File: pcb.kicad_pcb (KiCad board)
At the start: 4 copper layers, 26 x 25.6 mm, 39 parts, among them J1 TC2030-NL, J2 Conn_01x04, P1 USB_C_Plug, SW1 BOOT, U1 WE-TVS-82400102, U2 TCAN1042HGVDQ1, U3 STM32G431CBUx, U9 AP2112K-3.3

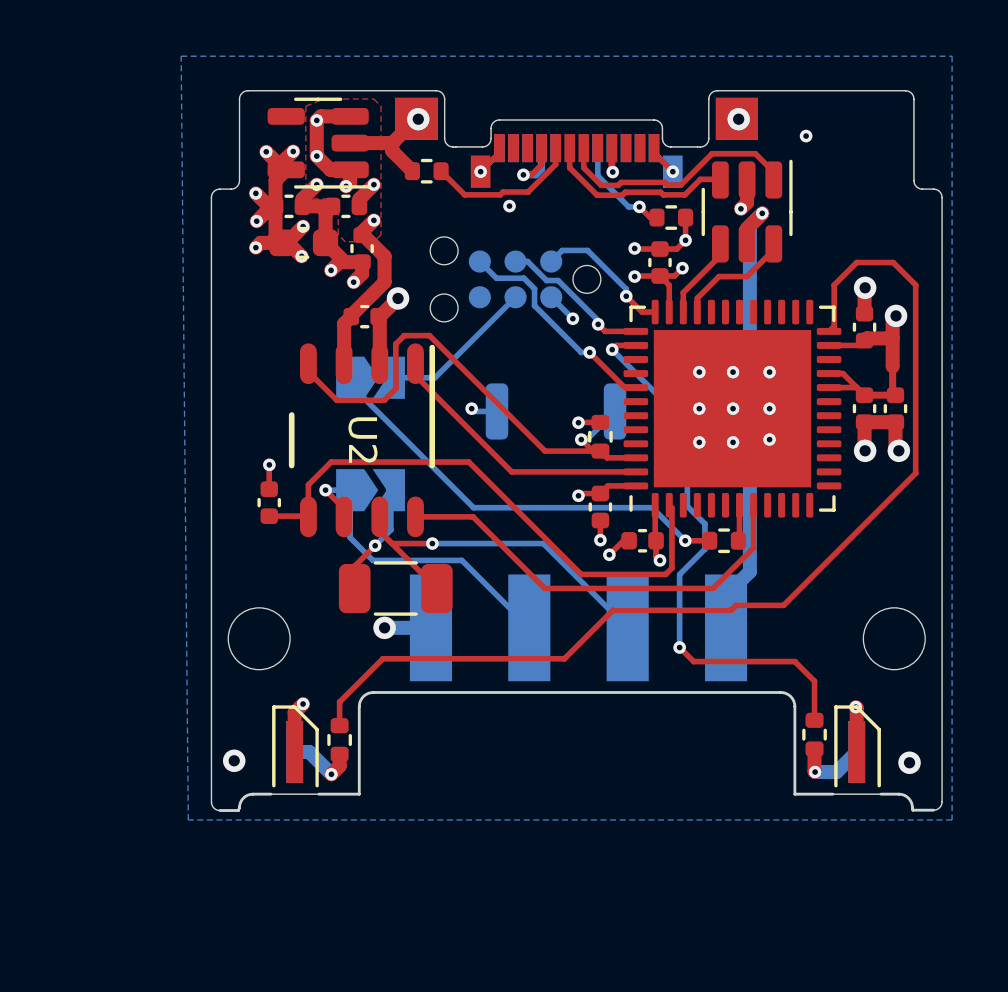
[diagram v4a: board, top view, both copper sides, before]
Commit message: clean up tracks/vias
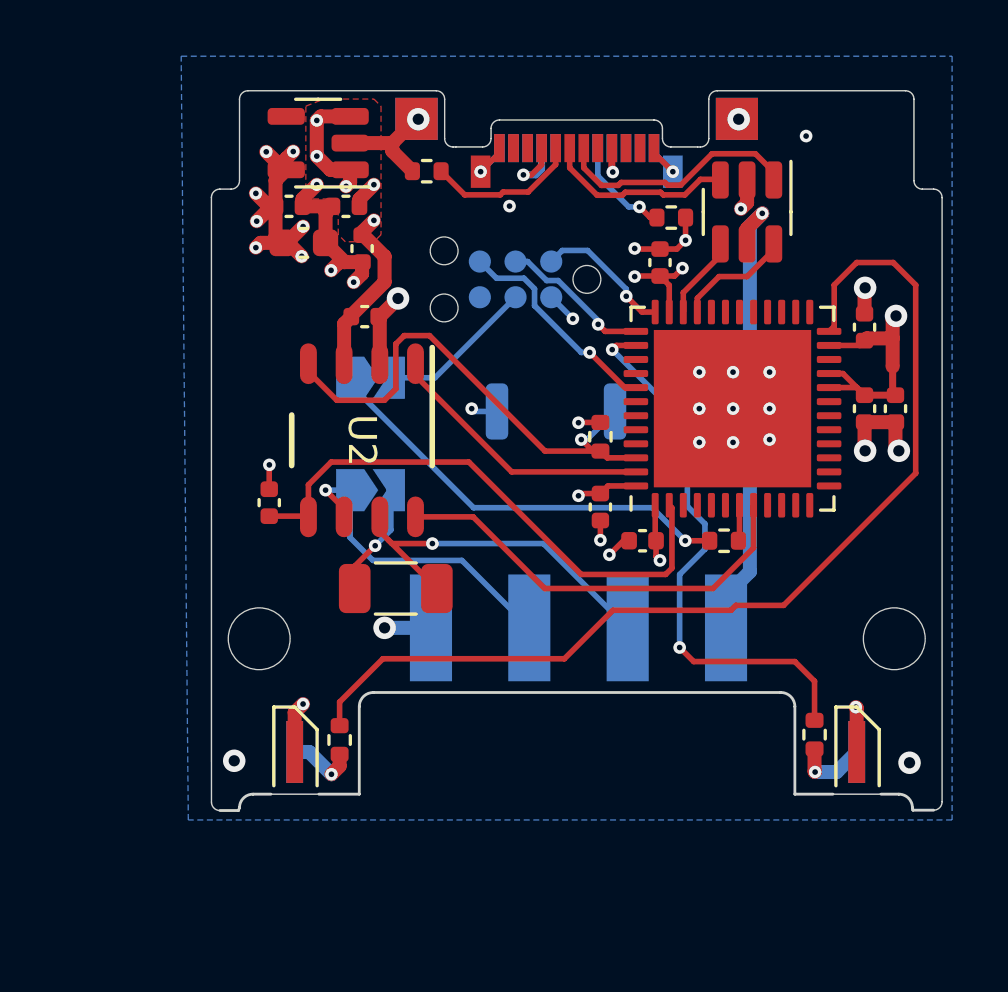
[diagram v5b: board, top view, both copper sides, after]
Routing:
- net VBUS: track 33.0 -> 31.7 mm
- net Net-(J2-Pin_3): track 13.2 -> 12.7 mm
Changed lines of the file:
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@@
   (segment (start 131.43 74.4) (end 130.79 73.76) (width 0.5) (layer "F.Cu") (net 2))
   (segment (start 144.66 87.6) (end 144.66 88.16) (width 0.2) (layer "F.Cu") (net 2))
-  (segment (start 151.91 80.65) (end 152.08 80.48) (width 0.2) (layer "F.Cu") (net 2))
   (segment (start 131.52 77) (end 132.1 76.42) (width 0.5) (layer "F.Cu") (net 2))
   (segment (start 131.35 77) (end 131.57 77) (width 0.5) (layer "F.Cu") (net 2))
@@
   (segment (start 144.8 78.18) (end 145.32 78.18) (width 0.2) (layer "F.Cu") (net 2))
   (segment (start 153.08 80.4) (end 152.16 80.4) (width 0.5) (layer "F.Cu") (net 2))
-  (segment (start 144.63 87.57) (end 144.66 87.6) (width 0.2) (layer "F.Cu") (net 2))
   (via (at 130.42 75.24) (size 0.45) (drill 0.2) (layers "F.Cu" "B.Cu") (net 2))
   (via (at 144.8 88.3) (size 0.45) (drill 0.2) (layers "F.Cu" "B.Cu") (net 2))
@@
   (segment (start 138.2 83) (end 138.1 82.9) (width 0.2) (layer "B.Cu") (net 2))
   (segment (start 140.935 78.935) (end 141.7 79.7) (width 0.2) (layer "B.Cu") (net 2))
-  (segment (start 140.93 78.935) (end 140.935 78.935) (width 0.2) (layer "B.Cu") (net 2))
   (segment (start 139 83) (end 138.2 83) (width 0.2) (layer "B.Cu") (net 2))
   (segment (start 152.08 82.42) (end 153.18 82.42) (width 0.25) (layer "F.Cu") (net 3))
@@
   (segment (start 151.31 81.65) (end 152.08 82.42) (width 0.2) (layer "F.Cu") (net 3))
   (segment (start 150.8175 81.65) (end 151.31 81.65) (width 0.2) (layer "F.Cu") (net 3))
-  (segment (start 153.08 82.32) (end 153.18 82.42) (width 0.25) (layer "F.Cu") (net 3))
   (segment (start 150.8175 82.15) (end 151.81 82.15) (width 0.2) (layer "F.Cu") (net 3))
-  (segment (start 134.242965 76.725) (end 134.2 76.725) (width 0.5) (layer "F.Cu") (net 4))
-  (segment (start 133.815 79.625001) (end 133.815 79.582036) (width 0.5) (layer "F.Cu") (net 4))
   (segment (start 133.775 74.4) (end 133.074 74.4) (width 0.5) (layer "F.Cu") (net 4))
   (segment (start 147.9 76.49) (end 147.9 77.0375) (width 0.5) (layer "F.Cu") (net 4))
@@
   (via (at 134.62 76.2) (size 0.45) (drill 0.2) (layers "F.Cu" "B.Cu") (net 4))
   (via (at 132.588 73.914) (size 0.45) (drill 0.2) (layers "F.Cu" "B.Cu") (net 4))
-  (segment (start 147.15 90.7) (end 147.15 89.55) (width 0.5) (layer "B.Cu") (net 4))
   (segment (start 140.385736 74.58) (end 139.94 74.58) (width 0.25) (layer "B.Cu") (net 4))
   (segment (start 143.087868 73.627868) (end 143.087868 74.447868) (width 0.2) (layer "B.Cu") (net 4))
@@
   (segment (start 145.13 86.3375) (end 145.225 86.4325) (width 0.2) (layer "F.Cu") (net 5))
   (segment (start 130.895 86.725001) (end 132.265002 86.725001) (width 0.2) (layer "F.Cu") (net 5))
-  (segment (start 132.265002 86.725001) (end 132.29 86.749999) (width 0.2) (layer "F.Cu") (net 5))
   (segment (start 145.225 86.4325) (end 145.225 88.575) (width 0.2) (layer "F.Cu") (net 5))
   (segment (start 138 84.8) (end 133.1 84.8) (width 0.2) (layer "F.Cu") (net 5))
@@
   (segment (start 143.688248 75.72) (end 142.587868 74.61962) (width 0.2) (layer "B.Cu") (net 22))
   (segment (start 142.587868 74.61962) (end 142.587868 73.627868) (width 0.2) (layer "B.Cu") (net 22))
-  (segment (start 146.95 77.0375) (end 146.95 77.45) (width 0.2) (layer "F.Cu") (net 26))
   (segment (start 146.95 77.45) (end 145.63 78.77) (width 0.2) (layer "F.Cu") (net 26))
   (segment (start 145.63 78.77) (end 145.63 79.4625) (width 0.2) (layer "F.Cu") (net 26))
   (segment (start 136.702157 87.700935) (end 135.263435 87.700935) (width 0.2) (layer "F.Cu") (net 27))
-  (segment (start 134.83 86.749999) (end 134.83 87.2675) (width 0.2) (layer "F.Cu") (net 27))
   (segment (start 135.263435 87.700935) (end 135.13125 87.56875) (width 0.2) (layer "F.Cu") (net 27))
   (segment (start 135.13125 87.56875) (end 136.8625 89.3) (width 0.2) (layer "F.Cu") (net 27))
@@
   (via (at 136.701222 87.7) (size 0.45) (drill 0.2) (layers "F.Cu" "B.Cu") (net 27))
   (segment (start 143.65 90.7) (end 140.65 87.7) (width 0.2) (layer "B.Cu") (net 27))
-  (segment (start 136.701222 87.7) (end 136.702157 87.700935) (width 0.2) (layer "B.Cu") (net 27))
   (segment (start 140.65 87.7) (end 136.701222 87.7) (width 0.2) (layer "B.Cu") (net 27))
   (segment (start 133.9375 88.504922) (end 133.9375 89.3) (width 0.2) (layer "F.Cu") (net 28))
@@
   (segment (start 135.225 87.217422) (end 135.225 85.8) (width 0.2) (layer "B.Cu") (net 28))
   (segment (start 135.7 80.3) (end 135.4 80.6) (width 0.2) (layer "F.Cu") (net 29))
-  (segment (start 132.29 81.59) (end 132.29 81.3) (width 0.2) (layer "F.Cu") (net 29))
   (segment (start 135.4 82.2) (end 135 82.6) (width 0.2) (layer "F.Cu") (net 29))
   (segment (start 142.68 84.41) (end 140.71 84.41) (width 0.2) (layer "F.Cu") (net 29))
@@
   (segment (start 142.2 84) (end 143.2 83) (width 0.2) (layer "B.Cu") (net 29))
   (segment (start 142 84) (end 142.2 84) (width 0.2) (layer "B.Cu") (net 29))
-  (segment (start 133.56 86.46) (end 133.56 86.749999) (width 0.2) (layer "F.Cu") (net 30))
   (segment (start 132.9 85.8) (end 133.56 86.46) (width 0.2) (layer "F.Cu") (net 30))
   (via (at 132.9 85.8) (size 0.45) (drill 0.2) (layers "F.Cu" "B.Cu") (net 30))
@@
   (segment (start 146.13 78.97) (end 146.9 78.2) (width 0.2) (layer "F.Cu") (net 31))
   (segment (start 146.13 79.4625) (end 146.13 78.97) (width 0.2) (layer "F.Cu") (net 31))
-  (segment (start 148.85 77.25) (end 148.85 77.0375) (width 0.2) (layer "F.Cu") (net 31))
   (segment (start 147.9 78.2) (end 148.85 77.25) (width 0.2) (layer "F.Cu") (net 31))
   (segment (start 146.9 78.2) (end 147.9 78.2) (width 0.2) (layer "F.Cu") (net 31))
-  (segment (start 147.63 87.56) (end 147.59 87.6) (width 0.2) (layer "F.Cu") (net 32))
   (segment (start 147.63 86.3375) (end 147.63 87.56) (width 0.2) (layer "F.Cu") (net 32))
   (segment (start 146 91.9) (end 149.6 91.9) (width 0.2) (layer "F.Cu") (net 33))
@@
   (segment (start 139.525 85.15) (end 143.9425 85.15) (width 0.2) (layer "F.Cu") (net 36))
   (segment (start 136.1 81.725) (end 139.525 85.15) (width 0.2) (layer "F.Cu") (net 36))
-  (segment (start 136.1 81.3) (end 136.1 81.725) (width 0.2) (layer "F.Cu") (net 36))
   (segment (start 148.13 87.853762) (end 146.683762 89.3) (width 0.2) (layer "F.Cu") (net 37))
   (segment (start 148.13 86.3375) (end 148.13 87.853762) (width 0.2) (layer "F.Cu") (net 37))
@@
   (via (at 145.7 87.6) (size 0.45) (drill 0.2) (layers "F.Cu" "B.Cu") (net 68))
   (segment (start 138.167156 86.425) (end 133.775 82.032844) (width 0.2) (layer "B.Cu") (net 68))
-  (segment (start 133.775 82.032844) (end 133.775 81.8) (width 0.2) (layer "B.Cu") (net 68))
   (segment (start 144.525 86.425) (end 138.167156 86.425) (width 0.2) (layer "B.Cu") (net 68))
   (segment (start 145.7 87.6) (end 144.525 86.425) (width 0.2) (layer "B.Cu") (net 68))
